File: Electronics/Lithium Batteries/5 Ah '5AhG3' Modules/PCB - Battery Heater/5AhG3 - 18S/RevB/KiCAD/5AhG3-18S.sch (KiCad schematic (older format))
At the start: 180 parts, among them J1 Conn_01x02

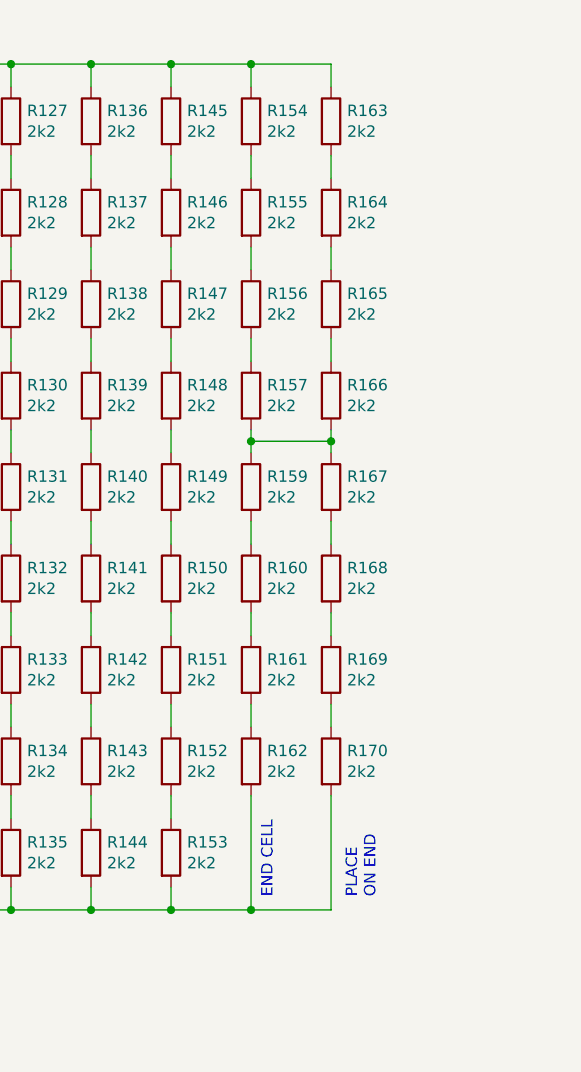
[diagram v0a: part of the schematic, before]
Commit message: RevB Heater PCBs, Daughterboard Schematic
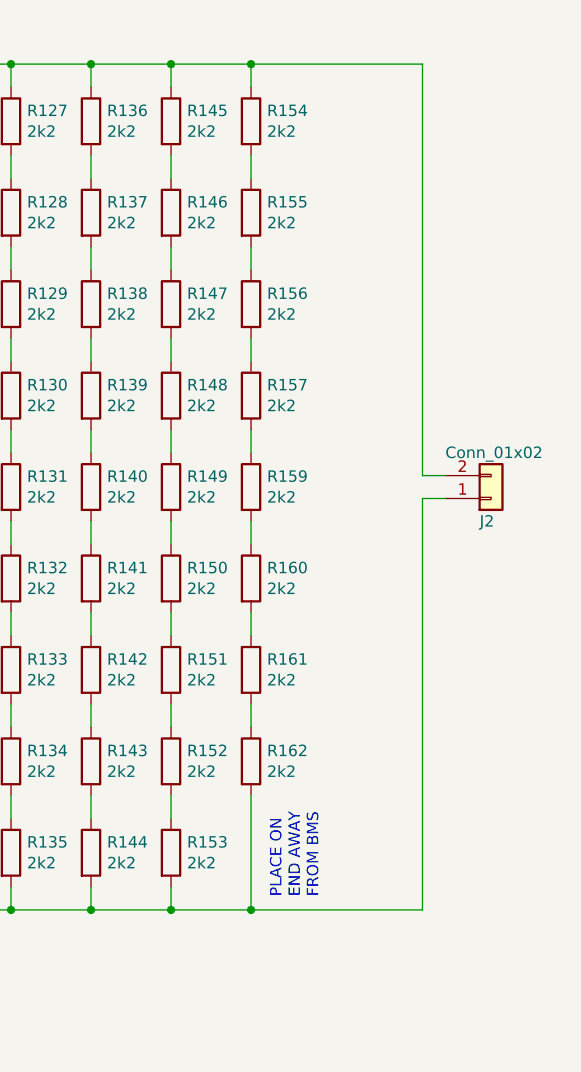
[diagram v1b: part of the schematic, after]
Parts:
- removed R163, R164, R165, R166, R167, R168, R169, R170: 2k2, Resistor_SMD:R_2010_5025Metric, symbol Device:R
- added J2: Conn_01x02, Connector_PinHeader_2.54mm:PinHeader_1x02_P2.54mm_Horizontal, symbol Connector_Generic:Conn_01x02
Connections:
- net HVDC_NEG: now also J2.1 (Pin_1)
- net HVDC_POS: now also J2.2 (Pin_2)
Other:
- note added: "PLACE ON\nEND AWAY\nFROM BMS"
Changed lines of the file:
@@
 	8450 2950 8450 3050
-Wire Wire Line
-	8450 3350 8450 3400
 Wire Wire Line
 	8450 3750 8450 3850
@@
 	1300 1750 2150 1750
 Connection ~ 2500 1750
-Wire Wire Line
-	8450 5450 8800 5450
-Connection ~ 8450 5450
-Connection ~ 8450 1750
-$Comp
-L Device:R R163
-U 1 1 638B7347
-P 8800 2000
-F 0 "R163" H 8870 2046 50  0000 L CNN
-F 1 "2k2" H 8870 1955 50  0000 L CNN
-F 2 "Resistor_SMD:R_2010_5025Metric" V 8730 2000 50  0001 C CNN
-F 3 "~" H 8800 2000 50  0001 C CNN
-	1    8800 2000
-	1    0    0    -1
-$EndComp
-$Comp
-L Device:R R164
-U 1 1 638B734D
-P 8800 2400
-F 0 "R164" H 8870 2446 50  0000 L CNN
-F 1 "2k2" H 8870 2355 50  0000 L CNN
-F 2 "Resistor_SMD:R_2010_5025Metric" V 8730 2400 50  0001 C CNN
-F 3 "~" H 8800 2400 50  0001 C CNN
-	1    8800 2400
-	1    0    0    -1
-$EndComp
-$Comp
-L Device:R R165
-U 1 1 638B7353
-P 8800 2800
-F 0 "R165" H 8870 2846 50  0000 L CNN
-F 1 "2k2" H 8870 2755 50  0000 L CNN
-F 2 "Resistor_SMD:R_2010_5025Metric" V 8730 2800 50  0001 C CNN
-F 3 "~" H 8800 2800 50  0001 C CNN
-	1    8800 2800
-	1    0    0    -1
-$EndComp
-$Comp
-L Device:R R166
-U 1 1 638B7359
-P 8800 3200
-F 0 "R166" H 8870 3246 50  0000 L CNN
-F 1 "2k2" H 8870 3155 50  0000 L CNN
-F 2 "Resistor_SMD:R_2010_5025Metric" V 8730 3200 50  0001 C CNN
-F 3 "~" H 8800 3200 50  0001 C CNN
-	1    8800 3200
-	1    0    0    -1
-$EndComp
-$Comp
-L Device:R R167
-U 1 1 638B735F
-P 8800 3600
-F 0 "R167" H 8870 3646 50  0000 L CNN
-F 1 "2k2" H 8870 3555 50  0000 L CNN
-F 2 "Resistor_SMD:R_2010_5025Metric" V 8730 3600 50  0001 C CNN
-F 3 "~" H 8800 3600 50  0001 C CNN
-	1    8800 3600
-	1    0    0    -1
-$EndComp
-$Comp
-L Device:R R168
-U 1 1 638B7365
-P 8800 4000
-F 0 "R168" H 8870 4046 50  0000 L CNN
-F 1 "2k2" H 8870 3955 50  0000 L CNN
-F 2 "Resistor_SMD:R_2010_5025Metric" V 8730 4000 50  0001 C CNN
-F 3 "~" H 8800 4000 50  0001 C CNN
-	1    8800 4000
-	1    0    0    -1
-$EndComp
-$Comp
-L Device:R R169
-U 1 1 638B736B
-P 8800 4400
-F 0 "R169" H 8870 4446 50  0000 L CNN
-F 1 "2k2" H 8870 4355 50  0000 L CNN
-F 2 "Resistor_SMD:R_2010_5025Metric" V 8730 4400 50  0001 C CNN
-F 3 "~" H 8800 4400 50  0001 C CNN
-	1    8800 4400
-	1    0    0    -1
-$EndComp
-$Comp
-L Device:R R170
-U 1 1 638B7371
-P 8800 4800
-F 0 "R170" H 8870 4846 50  0000 L CNN
-F 1 "2k2" H 8870 4755 50  0000 L CNN
-F 2 "Resistor_SMD:R_2010_5025Metric" V 8730 4800 50  0001 C CNN
-F 3 "~" H 8800 4800 50  0001 C CNN
-	1    8800 4800
-	1    0    0    -1
-$EndComp
-Wire Wire Line
-	8800 2250 8800 2150
-Wire Wire Line
-	8800 2550 8800 2650
-Wire Wire Line
-	8800 2950 8800 3050
-Wire Wire Line
-	8800 3350 8800 3400
-Wire Wire Line
-	8800 3750 8800 3850
-Wire Wire Line
-	8800 4150 8800 4250
-Wire Wire Line
-	8800 4550 8800 4650
 $Comp
 L Device:R R171
@@
 	2150 1850 2150 1750
 Wire Wire Line
-	8800 1850 8800 1750
-Wire Wire Line
-	8800 1750 8450 1750
-Wire Wire Line
 	2150 4950 2150 5450
-Wire Wire Line
-	8800 4950 8800 5450
-Text Notes 9000 5400 1    50   ~ 0
-PLACE\nON END
+Text Notes 8750 5400 1    50   ~ 0
+PLACE ON\nEND AWAY\nFROM BMS
 Text Notes 2350 5400 1    50   ~ 0
 PLACE\nON END
@@
 Text Notes 2600 5400 1    50   ~ 0
 END CELL
-Text Notes 8550 5400 1    50   ~ 0
-END CELL
 Wire Wire Line
 	2150 3400 2500 3400
@@
 	2500 3400 2500 3450
 Wire Wire Line
-	8450 3400 8800 3400
-Connection ~ 8450 3400
-Wire Wire Line
-	8450 3400 8450 3450
-Connection ~ 8800 3400
-Wire Wire Line
-	8800 3400 8800 3450
+	8450 3350 8450 3450
+$Comp
+L Connector_Generic:Conn_01x02 J2
+U 1 1 63A1C147
+P 9500 3650
+F 0 "J2" H 9450 3750 50  0000 L CNN
+F 1 "Conn_01x02" H 9300 3450 50  0000 L CNN
+F 2 "Connector_PinHeader_2.54mm:PinHeader_1x02_P2.54mm_Horizontal" H 9500 3650 50  0001 C CNN
+F 3 "~" H 9500 3650 50  0001 C CNN
+	1    9500 3650
+	1    0    0    1
+$EndComp
+Wire Wire Line
+	9300 3550 9200 3550
+Wire Wire Line
+	9200 3550 9200 1750
+Wire Wire Line
+	9200 1750 8450 1750
+Connection ~ 8450 1750
+Wire Wire Line
+	9300 3650 9200 3650
+Wire Wire Line
+	9200 3650 9200 5450
+Wire Wire Line
+	9200 5450 8450 5450
+Connection ~ 8450 5450
 $EndSCHEMATC
